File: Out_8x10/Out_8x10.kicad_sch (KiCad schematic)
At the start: 68 parts, among them J1 Conn_01x06, J2 nmount SW Debug, J3 USB_C_Receptacle_USB2.0, J4 Conn_01x06, SW1 Reset, SW2 Boot, SW3 ADDRESS, U1 ADM3483, U2 W25Q128JVSIQ, U3 RP2040, U4 SN74AHCT1G125, U5 AP2112K-3.3, Y1 12MHz,18pF

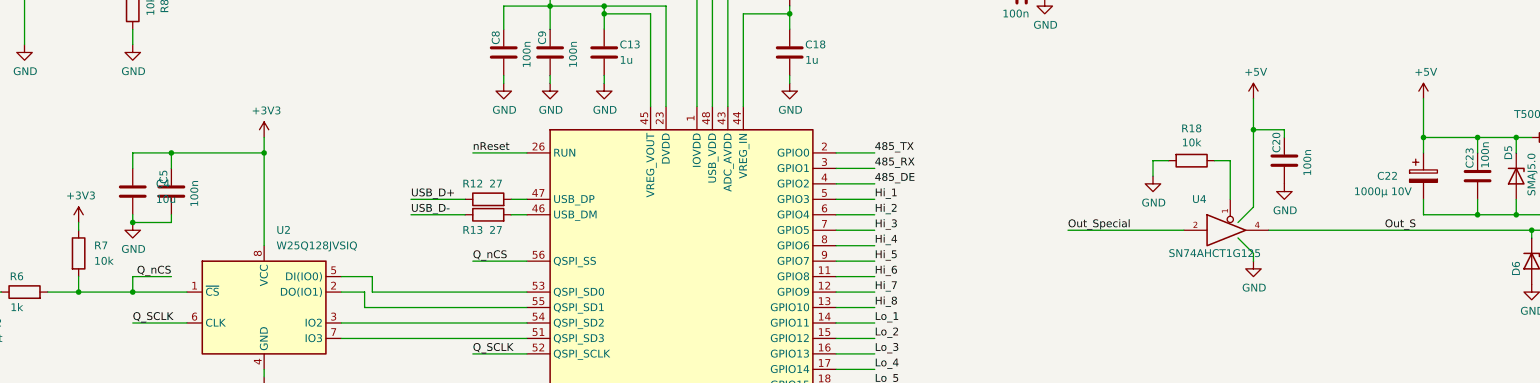
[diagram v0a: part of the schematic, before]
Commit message: updated layout
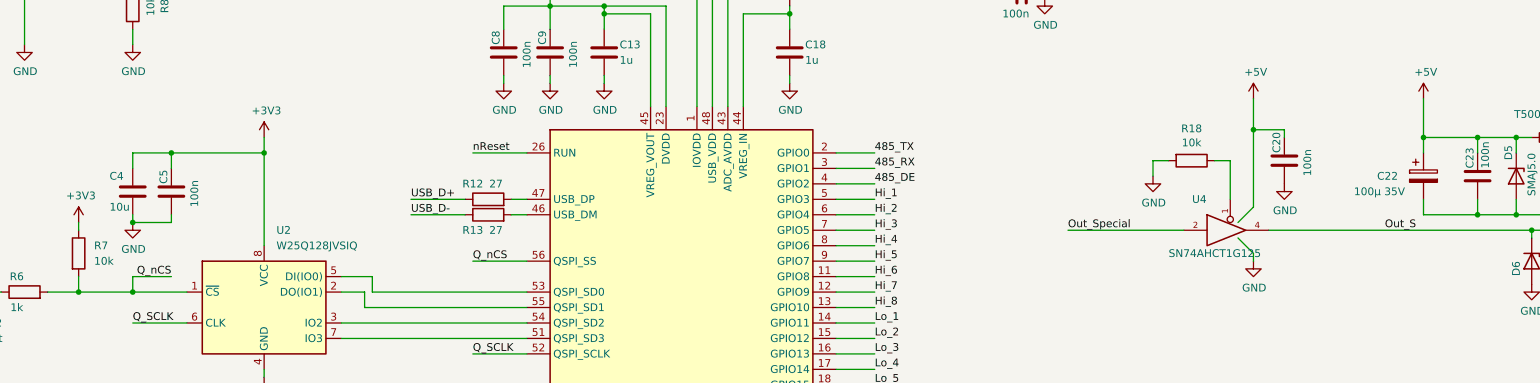
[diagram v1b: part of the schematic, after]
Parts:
- C22: value 1000µ 10V -> 100µ 35V; footprint Capacitor_THT:CP_Radial_D10.0mm_P5.00mm -> Capacitor_SMD:CP_Elec_6.3x7.7
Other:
- title: (none) -> Out_8x10
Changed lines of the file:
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@@
 (kicad_sch (version 20211123) (generator eeschema)
   (paper "A3")
+  (title_block
+    (title "Out_8x10")
+    (date "2023-10-08")
+    (rev "0.01")
+  )
   (junction (at 201.93 52.07) (diameter 0) (color 0 0 0 0)
   )
@@
       (effects (font (size 1.27 1.27)) (justify left))
     )
-    (property "Value" "1000µ 10V" (id 1) (at 309.88 102.87 0)
+    (property "Value" "100µ 35V" (id 1) (at 309.88 102.87 0)
       (effects (font (size 1.27 1.27)) (justify left))
     )
-    (property "Footprint" "Capacitor_THT:CP_Radial_D10.0mm_P5.00mm" (id 2) (at 322.2752 104.14 0)
+    (property "Footprint" "Capacitor_SMD:CP_Elec_6.3x7.7" (id 2) (at 322.2752 104.14 0)
       (effects (font (size 1.27 1.27)) hide)
     )
@@
   )
   (symbol (lib_id "Device:C") (at 109.22 102.87 0) (unit 1)
-    (in_bom yes) (on_board yes) (fields_autoplaced)
-    (property "Reference" "C4" (id 0) (at 113.03 101.5999 0)
+    (in_bom yes) (on_board yes)
+    (property "Reference" "C4" (id 0) (at 105.41 100.33 0)
       (effects (font (size 1.27 1.27)) (justify left))
     )
-    (property "Value" "10u" (id 1) (at 113.03 104.1399 0)
+    (property "Value" "10u" (id 1) (at 105.41 105.41 0)
       (effects (font (size 1.27 1.27)) (justify left))
     )
@@
       (reference "#G3") (unit 1) (value "LOGO") (footprint "")
     )
+    (path "/c9a975b0-1246-4730-bd1c-268dfbd64e4d/0daeebf0-a4fb-4230-9f74-d7595247a400"
+      (reference "#PWR01") (unit 1) (value "GND") (footprint "")
+    )
     (path "/35673b8a-3440-4c63-aade-4d916166039b"
       (reference "#PWR0101") (unit 1) (value "GND") (footprint "")
@@
     )
     (path "/c91e8187-5cdb-48c3-a93b-6176cb058619"
-      (reference "C22") (unit 1) (value "1000µ 10V") (footprint "Capacitor_THT:CP_Radial_D10.0mm_P5.00mm")
+      (reference "C22") (unit 1) (value "100µ 35V") (footprint "Capacitor_SMD:CP_Elec_6.3x7.7")
     )
     (path "/5c24d363-7f11-462b-a0b1-6ba7cbda5c4e"
@@
       (reference "C40") (unit 1) (value "1u 50V") (footprint "Capacitor_SMD:C_0603_1608Metric")
     )
+    (path "/c9a975b0-1246-4730-bd1c-268dfbd64e4d/a5fed3ff-44b4-4c21-b363-7f50b0b139b2"
+      (reference "C41") (unit 1) (value "100µ 35V") (footprint "Capacitor_SMD:CP_Elec_6.3x7.7")
+    )
     (path "/120b1f37-0d67-4515-b71d-37957a82cacf"

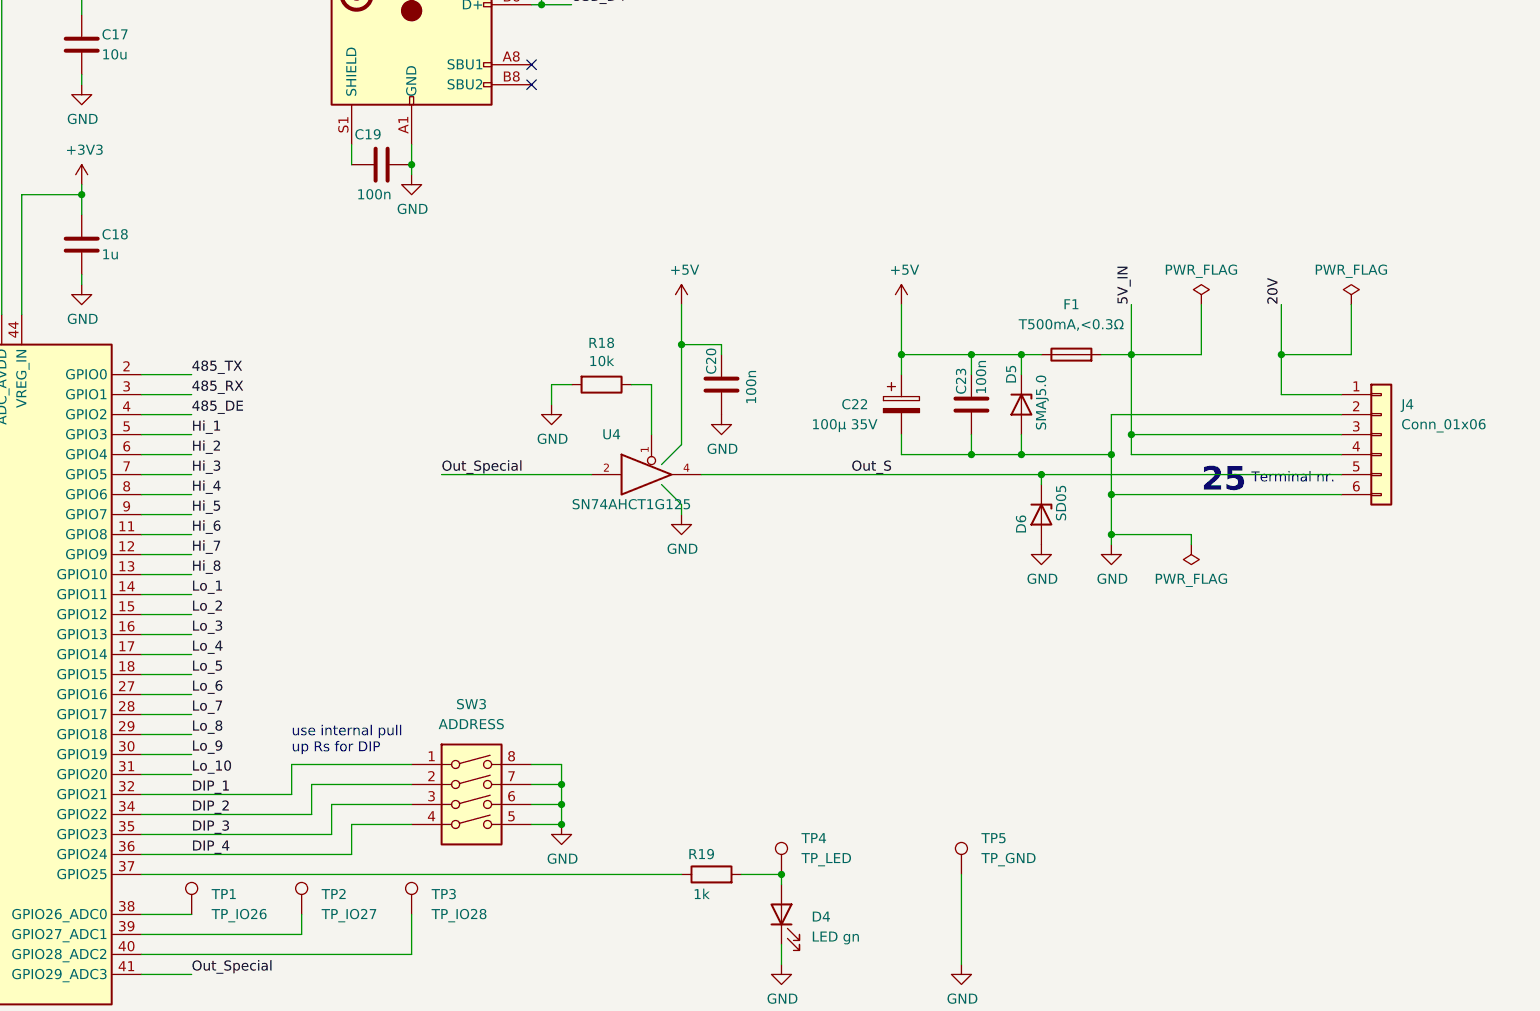
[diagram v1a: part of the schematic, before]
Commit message: updated layout
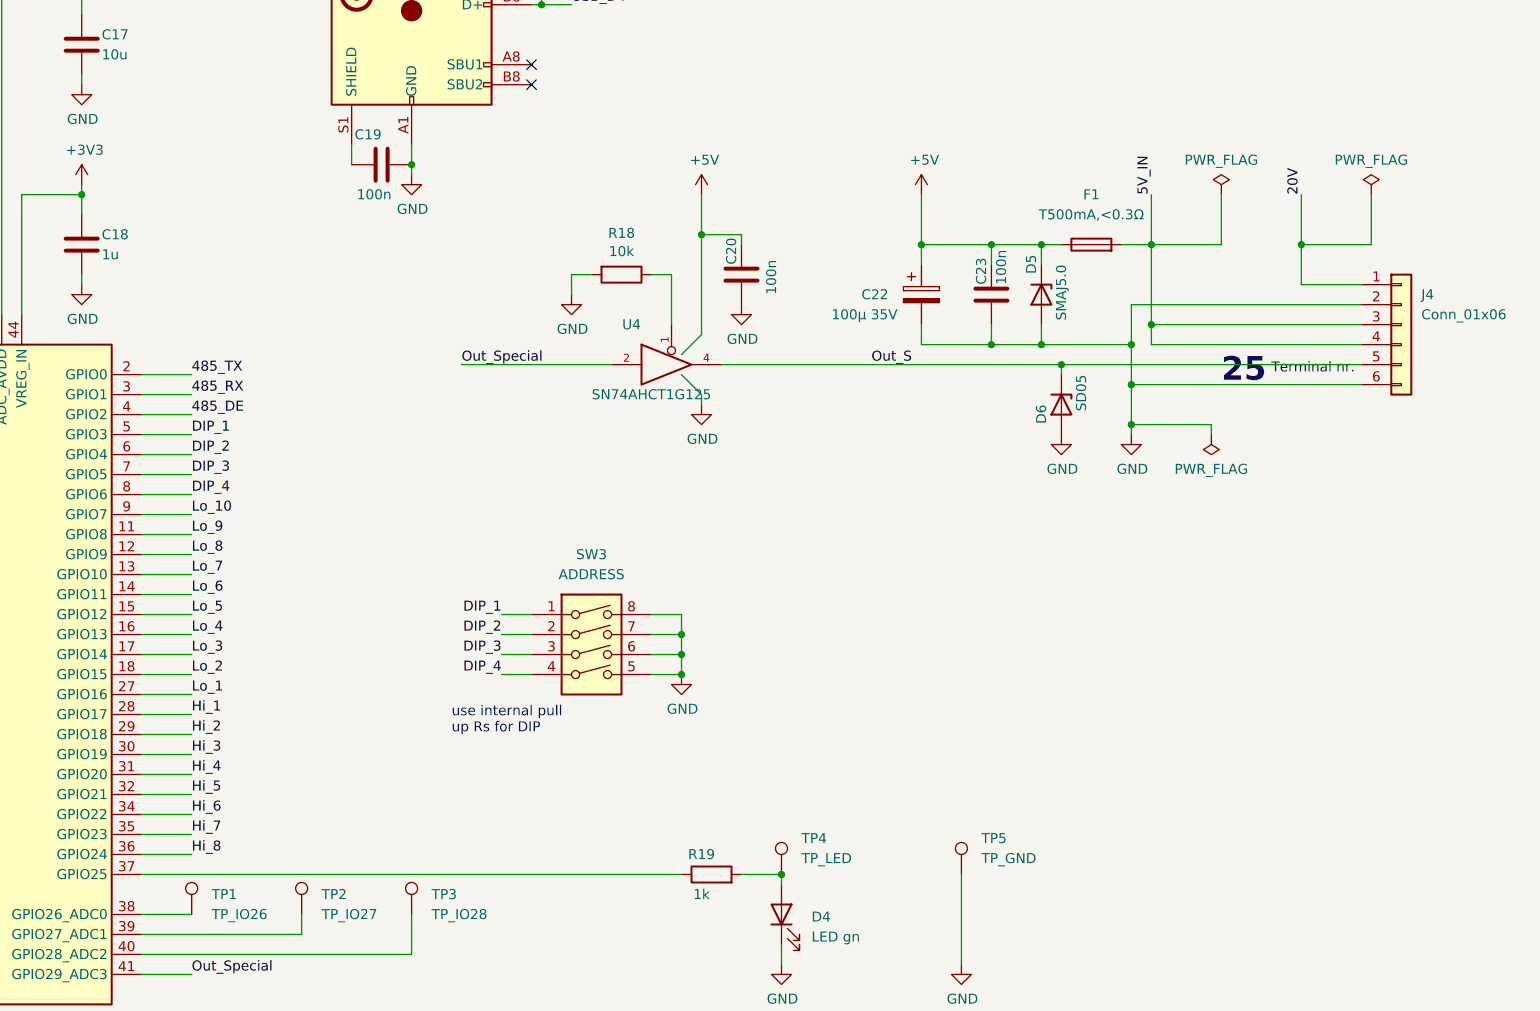
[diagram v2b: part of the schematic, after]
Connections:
- net DIP_1: now also U3.5 (GPIO3); no longer U3.32 (GPIO21)
- net DIP_2: now also U3.6 (GPIO4); no longer U3.34 (GPIO22)
- net DIP_3: now also U3.7 (GPIO5); no longer U3.35 (GPIO23)
- net DIP_4: now also U3.8 (GPIO6); no longer U3.36 (GPIO24)
- net Hi_1: now also U3.28 (GPIO17); no longer U3.5 (GPIO3)
- net Hi_2: now also U3.29 (GPIO18); no longer U3.6 (GPIO4)
- net Hi_3: now also U3.30 (GPIO19); no longer U3.7 (GPIO5)
- net Hi_4: now also U3.31 (GPIO20); no longer U3.8 (GPIO6)
- net Hi_5: now also U3.32 (GPIO21); no longer U3.9 (GPIO7)
- net Hi_6: now also U3.34 (GPIO22); no longer U3.11 (GPIO8)
- net Hi_7: now also U3.35 (GPIO23); no longer U3.12 (GPIO9)
- net Hi_8: now also U3.36 (GPIO24); no longer U3.13 (GPIO10)
- net Lo_1: now also U3.27 (GPIO16); no longer U3.14 (GPIO11)
- net Lo_10: now also U3.9 (GPIO7); no longer U3.31 (GPIO20)
- net Lo_2: now also U3.18 (GPIO15); no longer U3.15 (GPIO12)
- net Lo_3: now also U3.17 (GPIO14); no longer U3.16 (GPIO13)
- net Lo_4: now also U3.16 (GPIO13); no longer U3.17 (GPIO14)
- net Lo_5: now also U3.15 (GPIO12); no longer U3.18 (GPIO15)
- net Lo_6: now also U3.14 (GPIO11); no longer U3.27 (GPIO16)
- net Lo_7: now also U3.13 (GPIO10); no longer U3.28 (GPIO17)
- net Lo_8: now also U3.12 (GPIO9); no longer U3.29 (GPIO18)
- net Lo_9: now also U3.11 (GPIO8); no longer U3.30 (GPIO19)
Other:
- moved on the sheet: C20, C22, C23, D5, D6, F1, J4, R18, SW3, U4

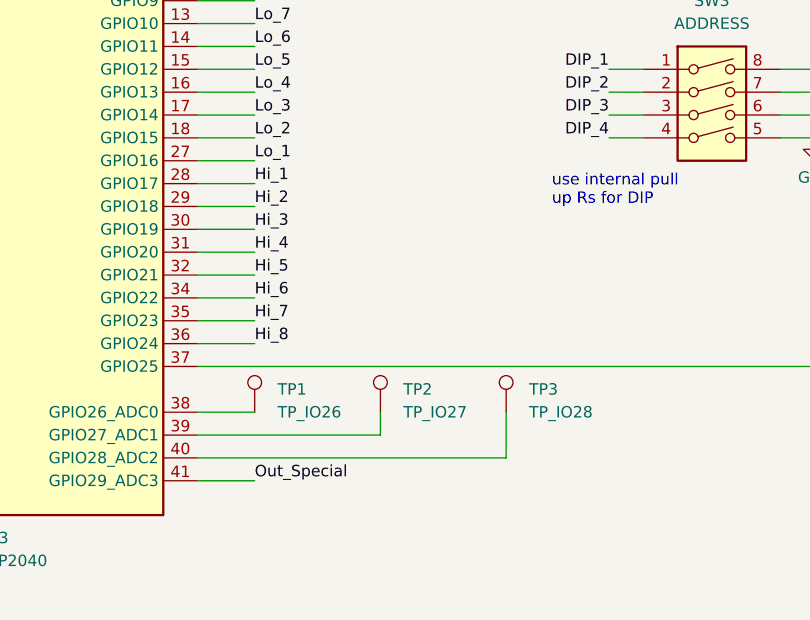
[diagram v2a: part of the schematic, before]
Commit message: updated layout
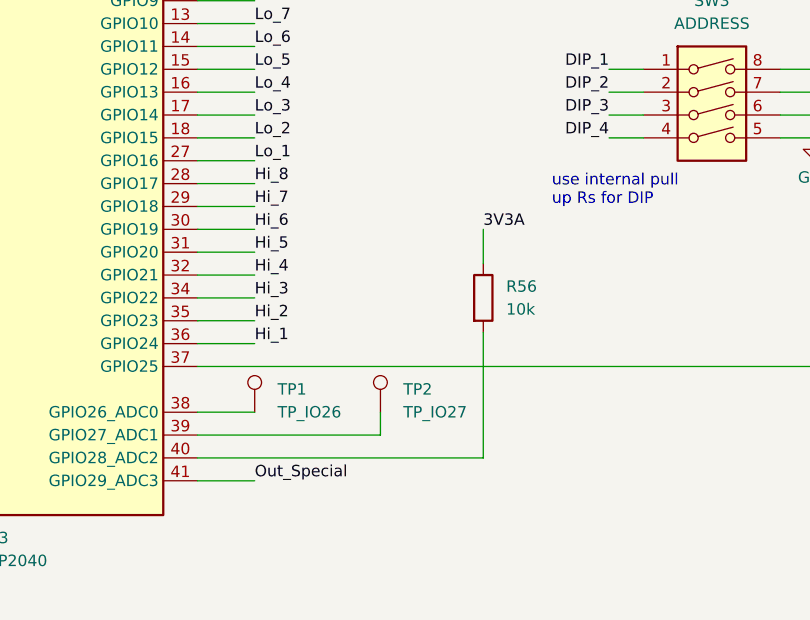
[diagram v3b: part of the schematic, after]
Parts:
- removed TP3: TP_IO28, Connector_Pin:Pin_D1.0mm_L10.0mm, symbol Connector:TestPoint
- added R56: 10k, Resistor_SMD:R_0603_1608Metric, symbol Device:R
- TP1, TP2: footprint Connector_Pin:Pin_D1.0mm_L10.0mm -> TestPoint:TestPoint_Pad_D1.0mm
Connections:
- net 3V3A: now also R56.1
- net Hi_1: now also U3.36 (GPIO24); no longer U3.28 (GPIO17)
- net Hi_2: now also U3.35 (GPIO23); no longer U3.29 (GPIO18)
- net Hi_3: now also U3.34 (GPIO22); no longer U3.30 (GPIO19)
- net Hi_4: now also U3.32 (GPIO21); no longer U3.31 (GPIO20)
- net Hi_5: now also U3.31 (GPIO20); no longer U3.32 (GPIO21)
- net Hi_6: now also U3.30 (GPIO19); no longer U3.34 (GPIO22)
- net Hi_7: now also U3.29 (GPIO18); no longer U3.35 (GPIO23)
- net Hi_8: now also U3.28 (GPIO17); no longer U3.36 (GPIO24)
- net at U3.40 (GPIO28_ADC2): now also R56.2
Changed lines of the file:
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@@
     (stroke (width 0) (type default) (color 0 0 0 0))
   )
+  (wire (pts (xy 256.54 144.78) (xy 256.54 148.59))
+    (stroke (width 0) (type default) (color 0 0 0 0))
+  )
   (wire (pts (xy 54.61 57.15) (xy 54.61 67.31))
     (stroke (width 0) (type default) (color 0 0 0 0))
@@
     (stroke (width 0) (type default) (color 0 0 0 0))
   )
-  (wire (pts (xy 259.08 165.1) (xy 259.08 170.18))
-    (stroke (width 0) (type default) (color 0 0 0 0))
-  )
   (wire (pts (xy 50.8 59.69) (xy 50.8 69.85))
     (stroke (width 0) (type default) (color 0 0 0 0))
@@
     (stroke (width 0) (type default) (color 0 0 0 0))
   )
-  (wire (pts (xy 224.79 170.18) (xy 259.08 170.18))
+  (wire (pts (xy 224.79 170.18) (xy 256.54 170.18))
     (stroke (width 0) (type default) (color 0 0 0 0))
   )
@@
     (stroke (width 0) (type default) (color 0 0 0 0))
   )
+  (wire (pts (xy 256.54 156.21) (xy 256.54 170.18))
+    (stroke (width 0) (type default) (color 0 0 0 0))
+  )
   (wire (pts (xy 91.44 34.29) (xy 91.44 38.1))
     (stroke (width 0) (type default) (color 0 0 0 0))
@@
     (effects (font (size 5 5) bold) (justify left bottom))
   )
-  (label "Hi_5" (at 231.14 149.86 0)
+  (label "Hi_5" (at 231.14 147.32 0)
     (effects (font (size 1.27 1.27)) (justify left bottom))
   )
@@
     (effects (font (size 1.27 1.27)) (justify right bottom))
   )
-  (label "Hi_2" (at 231.14 142.24 0)
+  (label "Hi_2" (at 231.14 154.94 0)
     (effects (font (size 1.27 1.27)) (justify left bottom))
   )
@@
     (effects (font (size 1.27 1.27)) (justify left bottom))
   )
-  (label "Hi_3" (at 231.14 144.78 0)
+  (label "Hi_3" (at 231.14 152.4 0)
     (effects (font (size 1.27 1.27)) (justify left bottom))
   )
@@
     (effects (font (size 1.27 1.27)) (justify right bottom))
   )
-  (label "Hi_4" (at 231.14 147.32 0)
+  (label "Hi_4" (at 231.14 149.86 0)
     (effects (font (size 1.27 1.27)) (justify left bottom))
   )
@@
     (effects (font (size 1.27 1.27)) (justify right bottom))
   )
+  (label "3V3A" (at 256.54 144.78 0)
+    (effects (font (size 1.27 1.27)) (justify left bottom))
+  )
   (label "5V_IN" (at 353.06 73.66 90)
     (effects (font (size 1.27 1.27)) (justify left bottom))
@@
     (effects (font (size 1.27 1.27)) (justify left bottom))
   )
-  (label "Hi_8" (at 231.14 157.48 0)
+  (label "Hi_8" (at 231.14 139.7 0)
     (effects (font (size 1.27 1.27)) (justify left bottom))
   )
@@
     (effects (font (size 1.27 1.27)) (justify left bottom))
   )
-  (label "Hi_1" (at 231.14 139.7 0)
+  (label "Hi_1" (at 231.14 157.48 0)
     (effects (font (size 1.27 1.27)) (justify left bottom))
   )
@@
     (effects (font (size 1.27 1.27)) (justify right bottom))
   )
-  (label "Hi_6" (at 231.14 152.4 0)
+  (label "Hi_6" (at 231.14 144.78 0)
     (effects (font (size 1.27 1.27)) (justify left bottom))
   )
@@
     (effects (font (size 1.27 1.27)) (justify left bottom))
   )
-  (label "Hi_7" (at 231.14 154.94 0)
+  (label "Hi_7" (at 231.14 142.24 0)
     (effects (font (size 1.27 1.27)) (justify left bottom))
   )
@@
     (pin "1")
   )
+  (symbol (lib_id "Device:R") (at 256.54 152.4 0) (unit 1)
+    (in_bom yes) (on_board yes) (fields_autoplaced)
+    (property "Reference" "R56" (id 0) (at 259.08 151.1299 0)
+      (effects (font (size 1.27 1.27)) (justify left))
+    )
+    (property "Value" "10k" (id 1) (at 259.08 153.6699 0)
+      (effects (font (size 1.27 1.27)) (justify left))
+    )
+    (property "Footprint" "Resistor_SMD:R_0603_1608Metric" (id 2) (at 254.762 152.4 90)
+      (effects (font (size 1.27 1.27)) hide)
+    )
+    (property "Datasheet" "~" (id 3) (at 256.54 152.4 0)
+      (effects (font (size 1.27 1.27)) hide)
+    )
+    (pin "1")
+    (pin "2")
+  )
   (symbol (lib_id "power:GND") (at 68.58 78.74 0) (unit 1)
     (in_bom yes) (on_board yes)
@@
       (effects (font (size 1.27 1.27)) (justify left))
     )
-    (property "Footprint" "Connector_Pin:Pin_D1.0mm_L10.0mm" (id 2) (at 236.22 165.1 0)
+    (property "Footprint" "TestPoint:TestPoint_Pad_D1.0mm" (id 2) (at 236.22 165.1 0)
       (effects (font (size 1.27 1.27)) hide)
     )
@@
     (pin "2")
   )
-  (symbol (lib_id "Connector:TestPoint") (at 259.08 165.1 0) (unit 1)
-    (in_bom yes) (on_board yes)
-    (property "Reference" "TP3" (id 0) (at 261.62 162.56 0)
-      (effects (font (size 1.27 1.27)) (justify left))
-    )
-    (property "Value" "TP_IO28" (id 1) (at 261.62 165.1 0)
-      (effects (font (size 1.27 1.27)) (justify left))
-    )
-    (property "Footprint" "Connector_Pin:Pin_D1.0mm_L10.0mm" (id 2) (at 264.16 165.1 0)
-      (effects (font (size 1.27 1.27)) hide)
-    )
-    (property "Datasheet" "~" (id 3) (at 264.16 165.1 0)
-      (effects (font (size 1.27 1.27)) hide)
-    )
-    (pin "1")
-  )
   (symbol (lib_id "power:GND") (at 50.8 132.08 0) (unit 1)
     (in_bom yes) (on_board yes)
@@
       (effects (font (size 1.27 1.27)) (justify left))
     )
-    (property "Footprint" "Connector_Pin:Pin_D1.0mm_L10.0mm" (id 2) (at 250.19 165.1 0)
+    (property "Footprint" "TestPoint:TestPoint_Pad_D1.0mm" (id 2) (at 250.19 165.1 0)
       (effects (font (size 1.27 1.27)) hide)
     )
@@
       (reference "R55") (unit 1) (value "100R") (footprint "Resistor_SMD:R_0603_1608Metric")
     )
+    (path "/2dfcc9cc-321e-4179-8d46-18226729f613"
+      (reference "R56") (unit 1) (value "10k") (footprint "Resistor_SMD:R_0603_1608Metric")
+    )
     (path "/995e13b5-c1cc-4580-b01d-8412c1b69470"
       (reference "SW1") (unit 1) (value "Reset") (footprint "Button_Switch_SMD:SW_SPST_SKQG_WithStem")
@@
     )
     (path "/6fc2dd83-1800-476d-a334-f121b9c51f01"
-      (reference "TP1") (unit 1) (value "TP_IO26") (footprint "Connector_Pin:Pin_D1.0mm_L10.0mm")
+      (reference "TP1") (unit 1) (value "TP_IO26") (footprint "TestPoint:TestPoint_Pad_D1.0mm")
     )
     (path "/a38a1aab-4402-498d-af5d-214a6bdd0d1d"
-      (reference "TP2") (unit 1) (value "TP_IO27") (footprint "Connector_Pin:Pin_D1.0mm_L10.0mm")
-    )
-    (path "/95f0479d-71ba-409c-9b11-472344073882"
-      (reference "TP3") (unit 1) (value "TP_IO28") (footprint "Connector_Pin:Pin_D1.0mm_L10.0mm")
+      (reference "TP2") (unit 1) (value "TP_IO27") (footprint "TestPoint:TestPoint_Pad_D1.0mm")
     )
     (path "/ddd8c900-4c7c-4ae4-ade4-c1575c4be8a8"
